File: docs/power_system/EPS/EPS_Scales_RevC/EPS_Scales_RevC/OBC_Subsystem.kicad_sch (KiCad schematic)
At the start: 28 parts, among them U10 INA230

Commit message: Layout Revisions
Organizing components and layering considerations
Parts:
- added J12: G125-MH11605L3P, RevC Footprints:HARWIN_G125-MH11605L3P, symbol 16 Pin Gecko Male Connector:G125-MH11605L3P
- U9: now not fitted; now left out of the parts list
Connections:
- net +3.3V_OBC: now also J12.1, J12.2, J12.3, J12.4
- net +3.3V_OBC_Out: now also J12.10, J12.9
- net GND: now also J12.17 (SH1), J12.18 (SH2), J12.5, J12.6, J12.7, J12.8
- net OBC SCL: now also J12.12
- net OBC SDA: now also J12.11
- net WDT_WDI_OBC: now also J12.15, J12.16
- net ~{OBC_TOGGLE_OBC}: now also J12.13, J12.14
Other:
- note added: "Gecko 16 pin Male connector"
- note added: "Gecko connector connects IMX8 to EPS"
- note removed: "OBC Dummy as placeholder for IMX8"
- moved on the sheet: C22, C23, C24, C25, C26, C27, C28, C29, C30, J5, L2, R29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

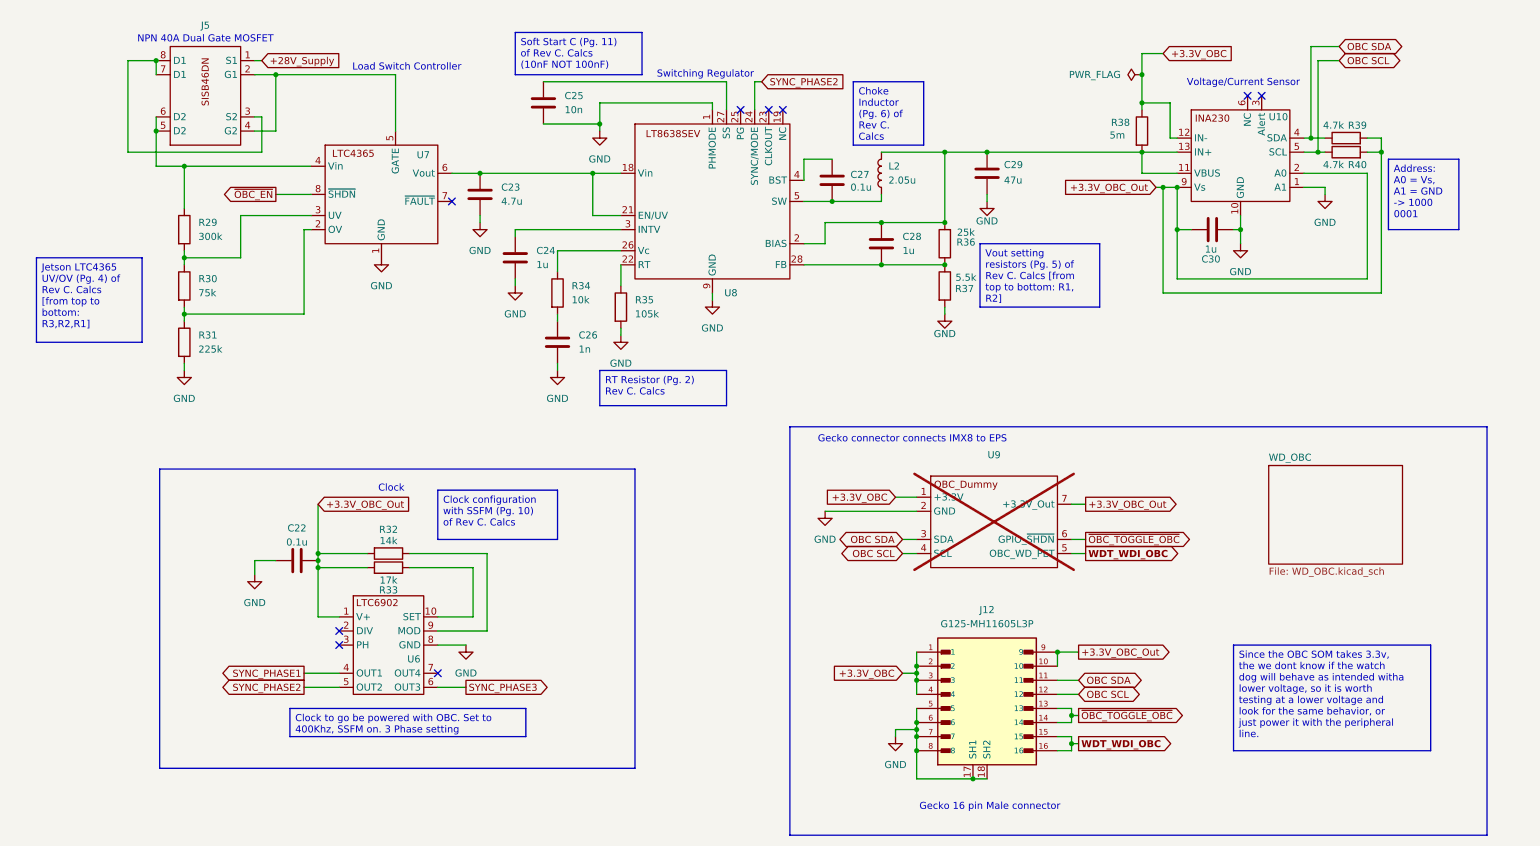
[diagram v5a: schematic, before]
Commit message: WIP REV C. Layout
Completed primary routing configuration.
Current orientation of components is for prototyping and does not reflect final layout.
Need further DRC checkings and track size correction for each sub-system.
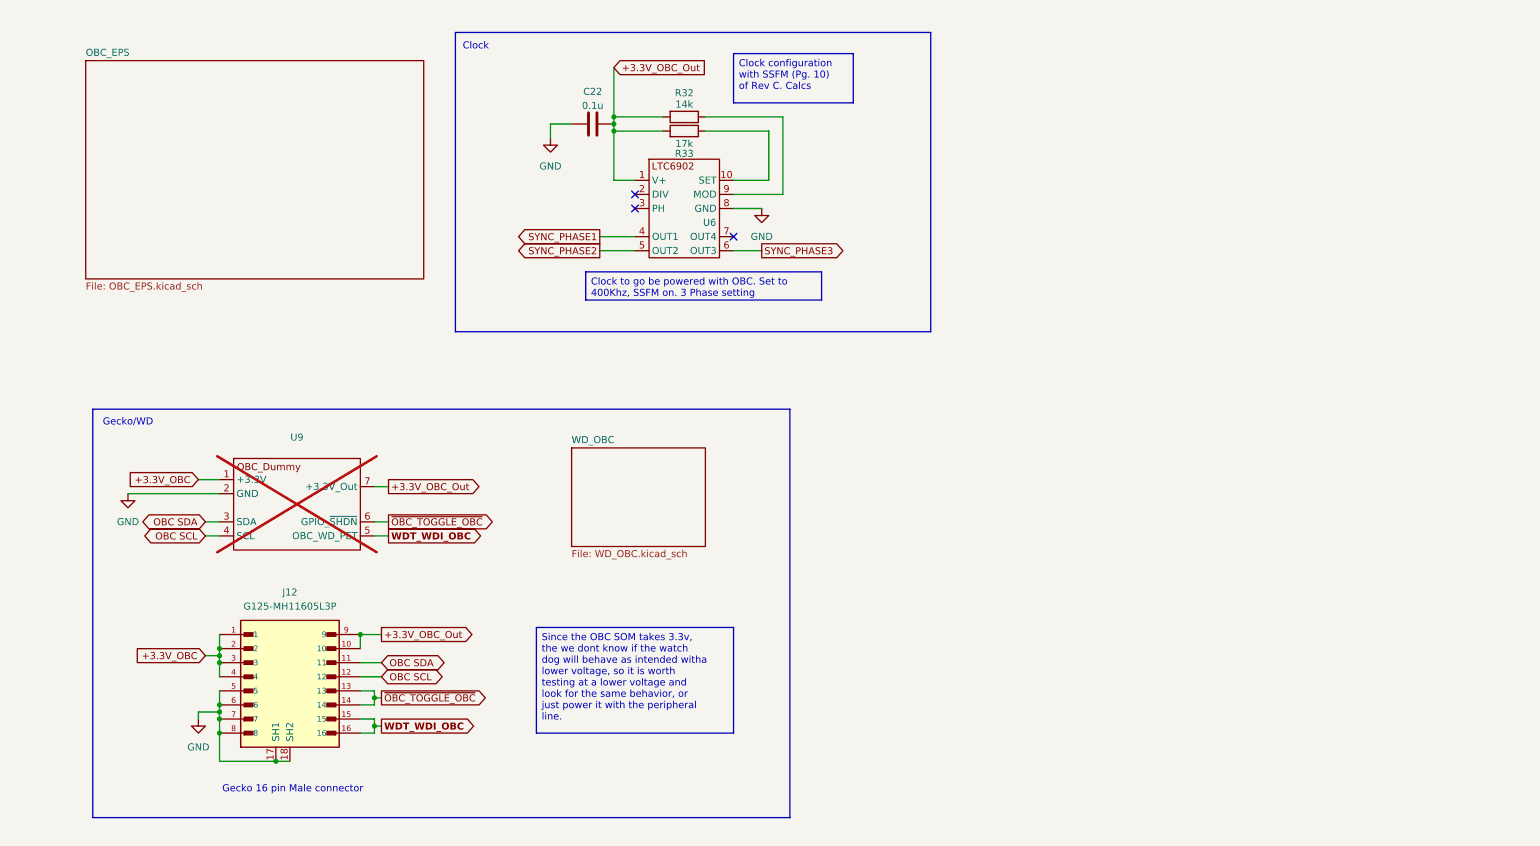
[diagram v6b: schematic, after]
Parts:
- removed C23: 4.7u, Capacitor_SMD:C_0603_1608Metric, symbol Device:C
- removed C24, C28, C30: 1u, Capacitor_SMD:C_0603_1608Metric, symbol Device:C
- removed C25: 10n, Capacitor_SMD:C_0603_1608Metric, symbol Device:C
- removed C26: 1n, Capacitor_SMD:C_0603_1608Metric, symbol Device:C
- removed C27: 0.1u, Capacitor_SMD:C_0603_1608Metric, symbol Device:C
- removed C29: 47u, Capacitor_SMD:C_0603_1608Metric, symbol Device:C
- removed J5: ~, RevC Footprints:SISB46DN-T1-GE3, symbol SISB46DN:SISB46DN
- removed L2: 2.05u, Inductor_SMD:L_0603_1608Metric, symbol Device:L
- removed R29: 300k, Resistor_SMD:R_0603_1608Metric, symbol Device:R
- removed R30: 75k, Resistor_SMD:R_0603_1608Metric, symbol Device:R
- removed R31: 225k, Resistor_SMD:R_0603_1608Metric, symbol Device:R
- removed R34: 10k, Resistor_SMD:R_0603_1608Metric, symbol Device:R
- removed R35: 105k, Resistor_SMD:R_0603_1608Metric, symbol Device:R
- removed R36: 25k, Resistor_SMD:R_0603_1608Metric, symbol Device:R
- removed R37: 5.5k, Resistor_SMD:R_0603_1608Metric, symbol Device:R
- removed R38: 5m, Resistor_SMD:R_0603_1608Metric, symbol Device:R
- removed R39, R40: 4.7k, Resistor_SMD:R_0603_1608Metric, symbol Device:R
- removed U10: INA230, RevC Footprints:INA230AIRGTT, symbol INA230:INA230 [RGT PACKAGE]
- removed U7: ~, RevC Footprints:LTC4365, symbol LTC4365:LTC4365
- removed U8: ~, RevC Footprints:LT8638SEVPBF, symbol LT8638SEV#PBF:LT863SEV#PBF
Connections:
- no-connect marks 9 -> 3
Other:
- added sheet OBC_EPS (OBC_EPS.kicad_sch)
- note added: "Gecko/WD"
- note removed: "Gecko connector connects IMX8 to EPS"
- note removed: "Load Switch Controller"
- note removed: "NPN 40A Dual Gate MOSFET"
- note removed: "Switching Regulator"
- note removed: "Voltage/Current Sensor"
- moved on the sheet: C22, J12, R32, R33, U6, U9

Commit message: WIP EPS REV C.
Removed XNOR implementation, redid layout for compactness, restarting routing for more efficient traces.
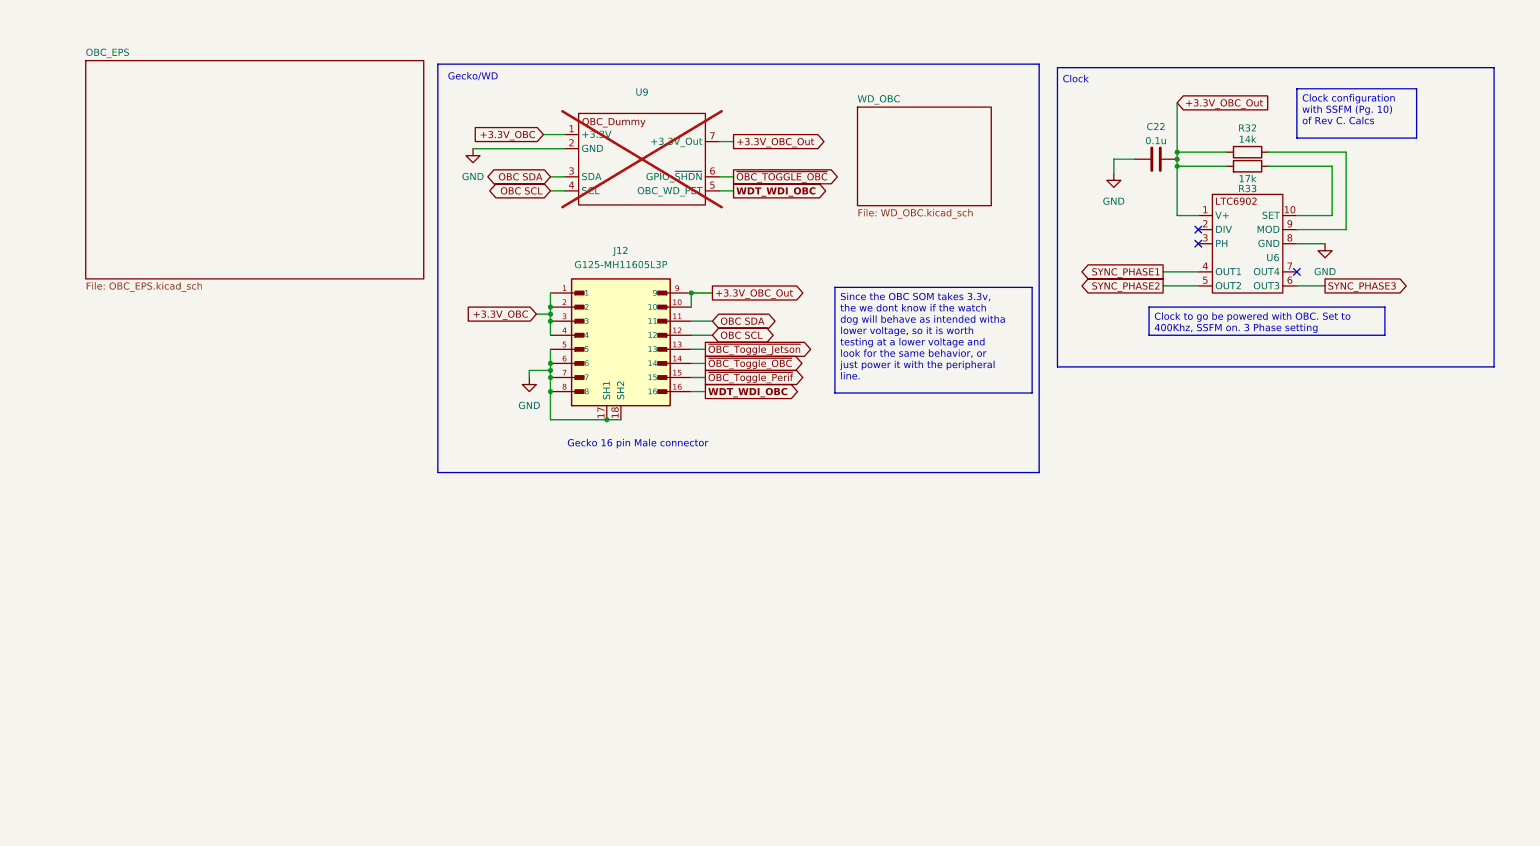
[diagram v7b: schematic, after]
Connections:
- net WDT_WDI_OBC: no longer J12.15
- net ~{OBC_TOGGLE_OBC}: no longer J12.13, J12.14
- new net ~{OBC_Toggle_Jetson}: J12.13
- new net ~{OBC_Toggle_OBC}: J12.14
- new net ~{OBC_Toggle_Perif}: J12.15
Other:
- moved on the sheet: C22, J12, R32, R33, U6, U9

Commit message: Layout and Routing DONE
Layout and Routing is complete, next step is DRC checking and making sure that the tracks and fab settings coincide with the settings we want to manufacture with.  Worth noting that we should probably get a version of this board with just one subsystem to test first before buying the whole thing.
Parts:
- J12: footprint RevC Footprints:HARWIN_G125-MH11605L3P -> RevC Footprints:CON16_2X8_UF_DF11
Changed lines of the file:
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@@
 			)
 		)
-		(property "Footprint" "RevC Footprints:HARWIN_G125-MH11605L3P"
+		(property "Footprint" "RevC Footprints:CON16_2X8_UF_DF11"
 			(at 123.19 73.66 0)
 			(effects
